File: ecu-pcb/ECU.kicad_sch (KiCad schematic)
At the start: 228 parts, among them J1 JTAG programming header, J3 USB-C receptacle, real Amphen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, J4 TE AMPSEAL 776180-1 (35-pos) 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, J5 TE AMPSEAL 776180-1 (35-pos) 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, J6 U.FL external BLE antenna con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, K1 Panasonic CB1a-T-P-12V automo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, Q1 SQM40020EL_GE3 automotive (AE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, Q10 FGP3040G2 automotive ignition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, Q11 PMV37ENEA automotive (AEC-Q10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, Q12 PMV37ENEA automotive (AEC-Q10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, Q13 PMV37ENEA automotive (AEC-Q10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, Q14 PMV37ENEA automotive (AEC-Q10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, Q15 PMV37ENEA automotive (AEC-Q10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, Q16 PMV37ENEA automotive (AEC-Q10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, Q17 PMV37ENEA automotive (AEC-Q10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, Q18 PMV37ENEA automotive (AEC-Q10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, Q2 PMV230ENEA automotive (AEC-Q1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, Q20 STD20NF06L VDD5 ext pass NMOS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, Q21 STD20NF06L VDD5 ext pass NMOS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, Q3 FGP3040G2 automotive ignition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, Q4 FGP3040G2 automotive ignition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, Q5 FGP3040G2 automotive ignition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, Q6 FGP3040G2 automotive ignition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, Q7 FGP3040G2 automotive ignition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, Q8 FGP3040G2 automotive ignition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, Q9 FGP3040G2 automotive ignition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, U1 NXP MPC5606B automotive (Qori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, U10 TLV2372-Q1 automotive (AEC-Q1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, U11 NXP TJA1043T automotive CAN t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, U12 NXP TJA1043T automotive CAN t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, U13 FTDI FT4232HA automotive (AEC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, U14 TI CC2640R2F-Q1 automotive BL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, U15 TI SN3257-Q1 automotive 4ch a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, U16 MAX9924 automotive (AEC-Q100)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, U17 TLV2372-Q1 automotive (AEC-Q1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, U18 Bosch CJ125 wideband O2 contr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, U19 AD8495ARZ EGT amp (industrial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, U2 LM74700-Q1 (AEC-Q100 G1), U20 MC33926 ETC H-bridge (industr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, U3 LMR33630-Q1 (AEC-Q100 G1), U4 TLV733P-Q1 (AEC-Q100 G1), U5 ST L9779WD-SPI automotive (Mu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, U6 ST L9779WD-SPI automotive (Mu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, U7 MAX9924 automotive (AEC-Q100)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, U8 MAX9924 automotive (AEC-Q100)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, U9 Bosch CJ125 wideband O2 contr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, Y1 8MHz (AEC-Q200), Y2 12MHz (AEC-Q200), Y3 24MHz (AEC-Q200)

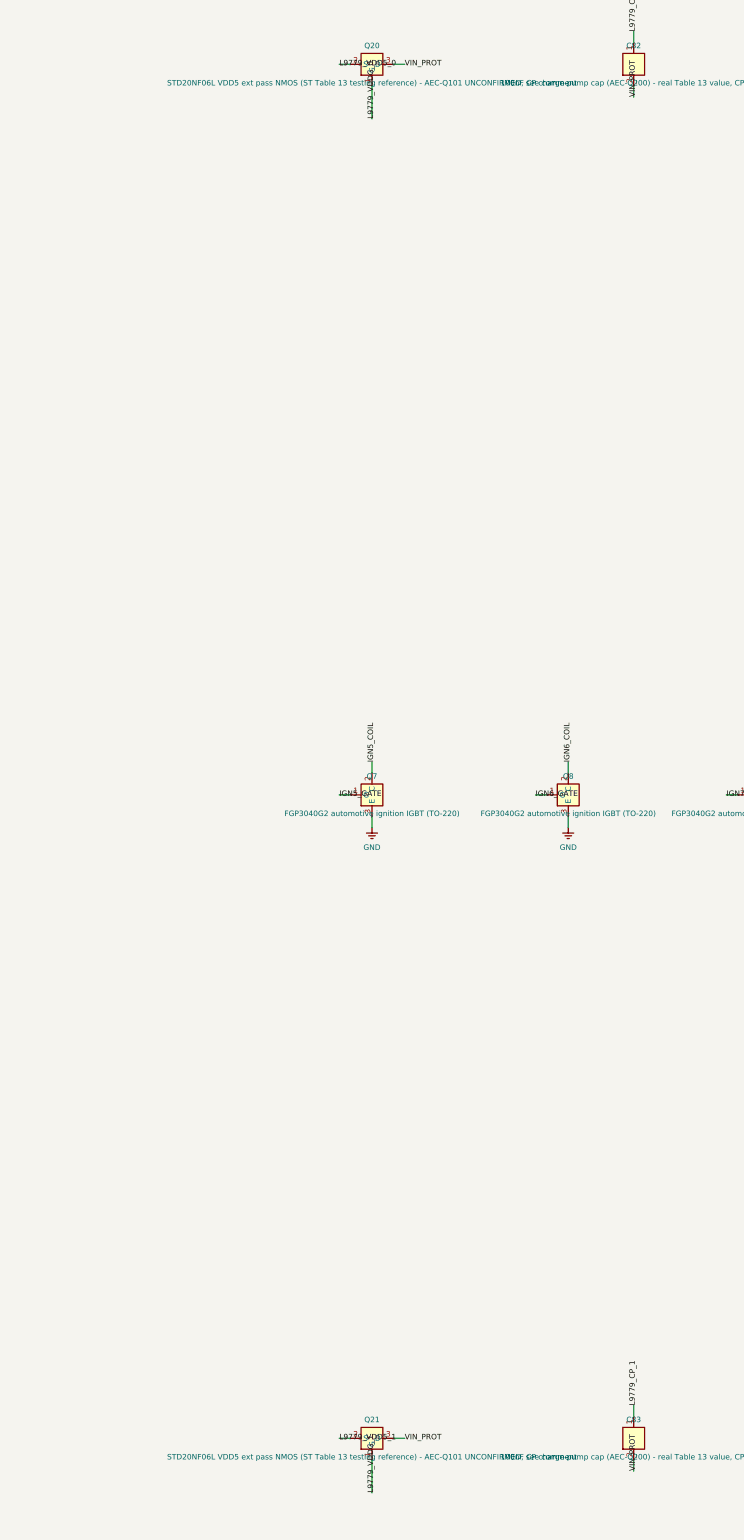
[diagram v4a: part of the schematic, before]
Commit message: Close two AEC qualification gaps; fix a package bug found doing it
MC33926: never actually unqualified. The revision this project had read
was Rev. 10.0 (2014, Freescale-era), which genuinely contains no AEC
statement - so the original flag was honest given the document in hand.
NXP's own revision history settles it: Rev. 13 (8/2018) records "Added
AEC-Q100 grade 1 qualified to Section 1 and Section 3", and Rev. 13+
state it twice. Real lesson recorded in the source: a missing
qualification statement can mean "not qualified" or "qualified in a
later revision than the one you happen to be reading".

L9779 VDD5 pass NMOS: ST makes an automotive-qualified version of the
very device it names as its own Table 13 testing reference -
STD20NF06LAG, AEC-Q101, same STripFET II process, voltage, RDS(on),
current and package, and it keeps the "L" logic-level gate the charge
pump depends on. That matters because ST warns a substitute needs
matching Vth and Ciss, since the FET sits inside the regulator's control
loop - the automotive grade of the exact tested device is the closest
possible match rather than a same-ratings lookalike.

Following that part number through caught a real bug: it had been placed
on MOSFET_N_BIG, a D2PAK (TO-263) footprint, but the whole STD20NF06L
family is DPAK (TO-252). Added a MOSFET_N_DPAK symbol.

st.com timed out on every attempt, so the AEC-Q101 status and package
rest on three independent corroborating sources rather than ST's own
PDF - flagged as such, and worth a direct check before fab.

AD8495 stays open and is not closeable by substitution - no AEC-Q100
thermocouple amplifier IC exists at all.

Board re-routed, DRC clean (18 known-benign warnings; the 2 unconnected
items are the same pre-existing U20 router residue).

Co-Authored-By: Claude Opus 5 <noreply@anthropic.com>
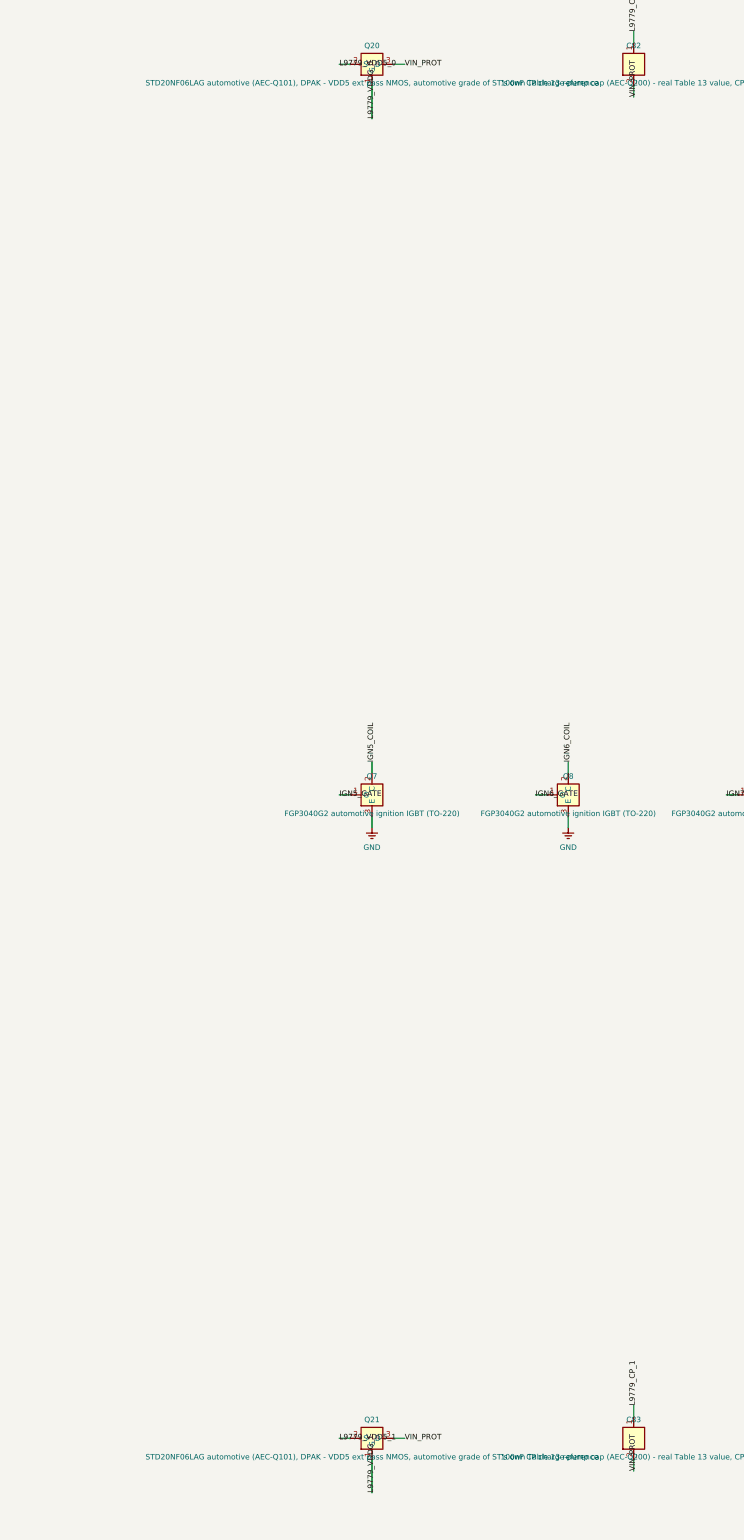
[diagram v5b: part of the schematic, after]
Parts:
- removed Q20, Q21: STD20NF06L VDD5 ext pass NMOS (ST Table 13 testin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, Package_TO_SOT_SMD:TO-263-3_TabPin2, symbol ECU:MOSFET_N_BIG
- added Q20, Q21: STD20NF06LAG automotive (AEC-Q101), DPAK - VDD5 e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, Package_TO_SOT_SMD:TO-252-3_TabPin2, symbol ECU:MOSFET_N_DPAK
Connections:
- net L9779_VDD5_0: now also Q20.2 (S)
- net L9779_VDD5_1: now also Q21.2 (S)
- net L9779_VDDG_0: now also Q20.1 (G)
- net L9779_VDDG_1: now also Q21.1 (G)
- net VIN_PROT: now also Q20.3 (D), Q21.3 (D)

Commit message: Replace AD8495 with ADS1118-Q1: board's last unqualified part
No AEC-Q100 dedicated thermocouple amplifier IC exists at all, so the
EGT channel could not be fixed by substitution - the fix had to be
architectural. A real AEC-Q100 Grade 1 ADC now reads the thermocouple
millivolts directly over SPI, with cold-junction compensation from its
own on-die sensor and linearisation moved into firmware. Same call the
sibling Thermo project made when it hit this identical tradeoff.

Front-end values are TI's own from the ADS1118 datasheet Figure 50
thermocouple application circuit, and TI's design rules were checked
rather than just the values copied: filter resistors under 1k (499R),
and C_DIFF at least 10x C_CM (1uF vs 100nF). The bias pull-up/pull-down
pair also gives free open-lead detection per TI's own text.

Moving EGT from analog to SPI freed exactly the pin the new device
needed for its chip select (PD[9], formerly PIN_ADC_EGT), so this cost
no new MCU or harness pin - siul2.c's earlier Table 4-1 check had
already established those Port D analog pads are GPIO-capable.

Two real driver findings: NOP[1:0] must be 01 or the device silently
ignores config writes entirely, and this part needs CPHA=1, so it
cannot share CJ125's CTAR despite both being slow enough.

Deliberately not faked: the ITS-90 type-K conversion is unimplemented.
NIST's own table download returns HTML rather than data, and this
project does not invent numeric constants from recall. SPI, config,
both raw reads and voltage scaling are complete; main.c stores the
thermocouple voltage and cold-junction temperature honestly rather than
computing a fabricated temperature. ads1118.h records the gap and the
two anchor points TI does confirm.

Also records a real negative result in build_pcb.py: routing stopped
reaching 0 unrouted as the board grew, so global spacing was tested as
the cause and ruled out - MARGIN 2.0->2.5 did not help and grew the
board ~28%, so it was reverted. The residual net is most often U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
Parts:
- removed U19: AD8495ARZ EGT amp (industrial grade - see registr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, Package_SO:MSOP-8_3x3mm_P0.65mm, symbol ECU:AD8495
- added C88: 1uF EGT TC differential (AEC-Q200) - real TI Fig 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, Capacitor_SMD:C_0603_1608Metric, symbol ECU:C_V
- added C89, C90: 100nF EGT TC common-mode (AEC-Q200) - real TI Fig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, Capacitor_SMD:C_0603_1608Metric, symbol ECU:C_V
- added R91: 1.00M EGT TC bias pull-down (AEC-Q200) - real TI 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, Resistor_SMD:R_0603_1608Metric, symbol ECU:R_V
- added R92, R93: 499R EGT TC series (AEC-Q200) - real TI Fig 50 RD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, Resistor_SMD:R_0603_1608Metric, symbol ECU:R_V
- added U19: ADS1118-Q1 EGT thermocouple ADC (AEC-Q100 Grade 1), TI_DGS0010A_VSSOP-10:TI_DGS0010A_VSSOP-10_3x3mm_P0.5mm, symbol ECU:ADS1118Q1
- C73: value 10nF EGT ADC filter (AEC-Q200) -> 100nF ADS1118-Q1 VDD decouple (AEC-Q200) - real TI Fig 50 value
- R77: value 10k EGT divider hi (AEC-Q200) -> 10k SPI_CS_EGT pull-up (AEC-Q200)
- R78: value 20k EGT divider lo (AEC-Q200) -> 1.00M EGT TC bias pull-up (AEC-Q200) - real TI Fig 50 value
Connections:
- net EGT_OUT is gone; now on net +3V3: R77.1
- net +3V3: now also C73.1, R78.1, U19.8 (VDD)
- net EGT_TC_M: now also R91.1, R93.1
- net EGT_TC_P: now also R78.2, R92.1
- net GND: now also C89.2, C90.2, R91.2, U19.3 (GND); no longer R78.2
- net SPI_SCLK: now also U19.1 (SCLK)
- net SPI_SI: now also U19.10 (DIN)
- net SPI_SO: now also U19.9 (DOUT)
- net EGT_ADC renamed SPI_CS_EGT
- net SPI_CS_EGT: now also U19.2 (CS); no longer C73.1, R78.1
- new net EGT_AIN0: C88.1, C89.1, R92.2, U19.4 (AIN0)
- new net EGT_AIN1: C88.2, C90.1, R93.2, U19.5 (AIN1)
- no-connect marks 144 -> 145

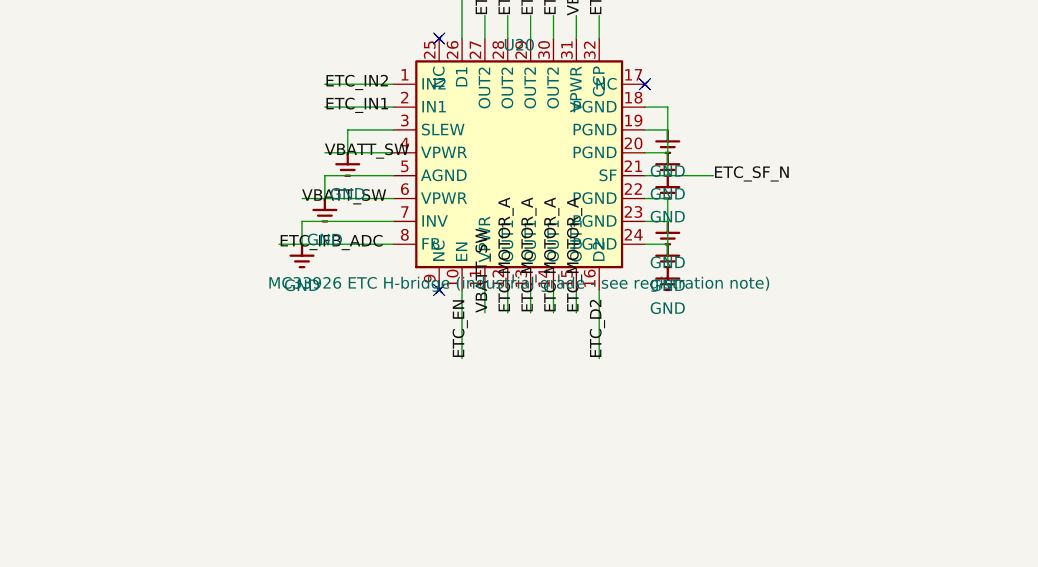
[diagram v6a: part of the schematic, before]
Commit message: Add generated BOM + parts-list page for jessiescars.com
68 orderable line items covering all 234 board placements. Generated
from ECU.kicad_sch by a new build_bom.py rather than hand-listed, for
the same reason everything else here is script-driven: this board had
five real part changes late in its life (MC33810 -> L9779WD-SPI, 16A
relay -> 40A Panasonic, AD8495 -> ADS1118-Q1, both temp sensors, a pass
NMOS package fix), and a hand-kept BOM drifts silently through every one
of them. A coverage assertion checks every schematic part lands on
exactly one BOM line - it immediately caught a double-count where fuse
elements were counted as placements rather than as separate orderable
items sharing the holders' four.

Honest about scope rather than overclaiming "distributor-verified":
actives, connectors and electromechanical parts carry real MPNs already
verified against manufacturer datasheets during design; passives are
specified parametrically (value, package, AEC-Q200) rather than pinned
to one vendor, which is how commodity passives are actually bought; and
no live pricing or stock was checked. CJ125 and the eight FGP3040G2
IGBTs are called out as the lines to confirm availability on first.

Also fixes a stale value string the BOM surfaced: U20 still described
the MC33926 as industrial grade after it was confirmed AEC-Q100 Grade 1.

Board re-routed: 0 unconnected, 18 known-benign warnings.

Co-Authored-By: Claude Opus 5 <noreply@anthropic.com>
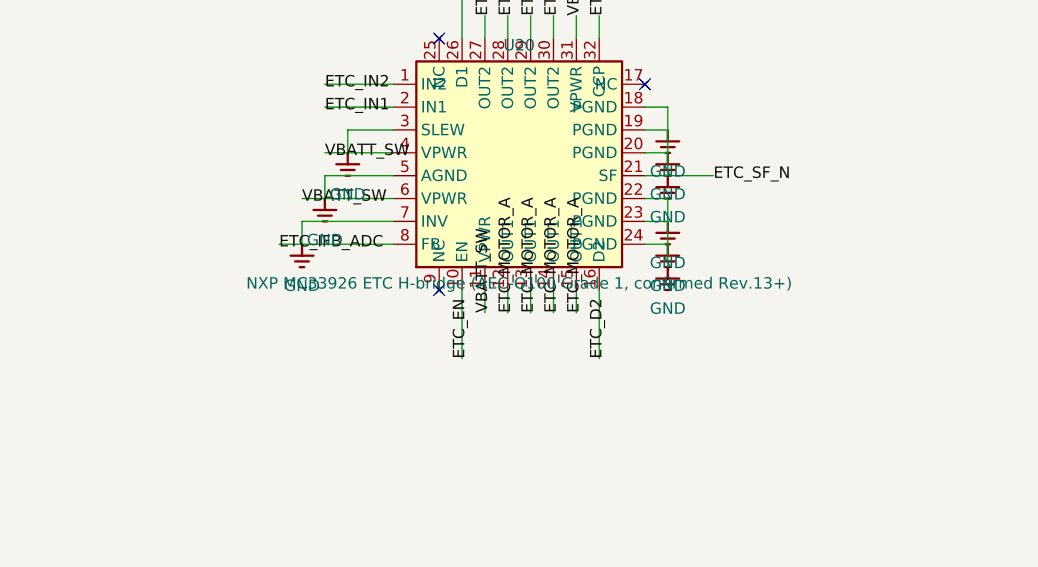
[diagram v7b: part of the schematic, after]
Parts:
- U20: value MC33926 ETC H-bridge (industrial grade - see registration note) -> NXP MC33926 ETC H-bridge (AEC-Q100 Grade 1, confirmed Rev.13+)

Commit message: Replace AD8495 with ADS1118-Q1: board's last unqualified part
Resolve the 2.4GHz balun - board's last placeholder part

FB1 is now Johanson 2450BM14G0011T-AEC, an impedance-matched integrated
balun + low-pass filter, taken from TI's own SWRA572 application report
for this exact CC26xx pairing and cross-checked against Johanson's AEC
datasheet. Every part on this board is now a real, specific part.

The suffix matters twice over. The plain 2450BM14G0011 is rated only
-40..+85C and would be genuinely out of spec here, so -AEC (-40..+105C,
AEC-Q200) is functionally required rather than a paperwork upgrade. And
2450BM15A0002, which searches kept surfacing, is a different part for
older CC253x-era chipsets entirely. Both noted on the BOM page, since
ordering the wrong one is easy and expensive.

Chosen over TI's nine-component discrete LC reference (CC2640R2F-Q1
Figure 9-1): SWRA572 states the integrated part consolidates exactly
those nine components with comparable RF performance, and nine
tight-tolerance 0402 RF parts is the wrong trade on a machine-routed
board. Its +105C also matches the CC2640R2F-Q1's own AEC-Q100 Grade 2
rating, so it adds no new thermal limit.

Checked rather than assumed: KiCad's bundled Balun_Johanson_1.6x0.8mm
looked like it split the differential pair across the part. Johanson's
own terminal drawing shows 3/2/1 and 4/5/6 along the long edges - the
same counter-clockwise order drawn portrait rather than landscape - so
BP1/BP2 stay adjacent. A balun with a split pair is a silent RF failure.

Adds a 100pF series DC block (C91) beyond TI's reference: the
CC2640R2F-Q1 datasheet requires one if the antenna has a DC path to
ground, the antenna is deliberately unchosen, and whether the balun
passes DC could not be confirmed. 100pF is ~0.7 ohm at 2.4GHz so it is
invisible - deliberately not TI's 12pF, which was part of the discrete
match itself.

Real remaining caveat is layout, not parts: the RF chain needs hand
routing, since FreeRouting has no conc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
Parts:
- added C91: 100pF RF DC block (AEC-Q200, C0G/NP0) - see comme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, Capacitor_SMD:C_0603_1608Metric, symbol ECU:C_V
- FB1: value 2.4GHz balun (typical - confirm part/matching before fab) -> Johanson 2450BM14G0011T-AEC balun+LPF (AEC-Q200, -40..+105C) - see registration note; footprint Package_DFN_QFN:DFN-6_1.6x1.3mm_P0.4mm -> RF_Converter:Balun_Johanson_1.6x0.8mm
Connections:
- net BLE_ANT: now also C91.2; no longer FB1.3 (OUT)
- net BLE_RF_N: now also FB1.3 (BP1); no longer FB1.2 (IN-)
- net BLE_RF_P: now also FB1.4 (BP2); no longer FB1.1 (IN+)
- net GND: now also FB1.5 (GND), FB1.6 (GND); no longer FB1.4 (GND)
- new net BLE_RF_OUT: C91.1, FB1.1 (UBP)
- no-connect marks 145 -> 146
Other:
- note added: "be autorouted, see the README. Hardware-forced MCU reset-into-"
- note added: "exact CC26xx pairing, AEC-Q200 and rated -40..+105C (the plain"
- note added: "integrated balun+LPF from TI's own SWRA572 app report for this"
- note added: "non-AEC part is only +85C and would be out of spec here). It"
- note added: "part - Johanson 2450BM14G0011T-AEC, an impedance-matched"
- note added: "replaces TI's 9-component discrete LC reference network. The RF"
- note added: "requirement); the BLE RF chain's balun is now a REAL, specific"
- note added: "section still needs HAND LAYOUT - a 2.4GHz matched line cannot"
- note removed: "TOPOLOGY (differential radio -> balun -> single-ended antenna)"
- note removed: "analog network in step 5. Hardware-forced MCU reset-into-"
- note removed: "but its exact part/matching-network VALUES are placeholder,"
- note removed: "pending TI's official reference-design BOM (not fetched this"
- note removed: "requirement); the BLE RF chain's balun is a real required"
- note removed: "session) - same 'topology real, values TBD' treatment as CJ125's"
